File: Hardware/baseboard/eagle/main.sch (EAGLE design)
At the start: 33 parts, among them U3.1 LSM9DS1, X1.0 ARDUINO_UNO, X1.2 TACH/LAP, X2.1 MOTOR

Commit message: stash, added some units
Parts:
- added C1.1: XX, rcl:C-EUC1210K
- added C4.XX1: 100nF, rcl:C-EUC0402K
- added C4.XX10: 2.2uF, rcl:C-EUC0603K
- added C4.XX11, C4.XX12: 100uF, kitt.psvs:CPOL-29172312
- added C4.XX2: 10uF, rcl:C-EUC0603
- added D1.1: (no value), diode:SCHOTTKY-DIODESMD
- added L1: NRS8030XX, kitt.psvs:NRS8030XX
- added L1.1, L2.2: BEAD, rcl:L-EUL4516C
- added R1, R2: (no value), rcl:R-EU_R0805W
- added R4.XX1, R4.XX4, R4.XX5: 100kR, rcl:R-EU_R0402
- added R4.XX2: 549kR, rcl:R-EU_R0402
- added R4.XX3: 90k9R, rcl:R-EU_R0402
- added U☢⏧: TPS61032RSARPSDO-G16, kitt.ic:TPS61032RSARPSDO-G16
- added X2.2: MOTOR, con-phoenix-254:MPT2
- added ☇4XX1⏧: PTR1TP07SQ, testpad:PTR1TP07SQ
- added ☈1, ☈2: (no value), jumper:SJ
- C3.2: value 10nF -> 100nF
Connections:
- removed net AGND: C2.1.2, C2.2.2, C2.3.-, C2.5.2, J2.1.1, U2.2.PGND
- removed net TH: U2.2.PAD
- new net +18V: D1.1.A, R1.2, X2.2-1.1
- new net +5V: L2.2.2
- new net N$1: L1.2, U☢⏧.SW, U☢⏧.SW_2
- new net N$10: U☢⏧.FB, ☇4XX1⏧.TP
- new net N$11: R1.1, R2.2, ☈2.1
- new net N$12: D1.1.C, L1.1.1
- new net N$5: R4.XX1.1, U☢⏧.LBI
- new net N$6: R4.XX2.1, U☢⏧.SYNC
- new net N$7: C4.XX10.1, C4.XX11.+, C4.XX12.+, L2.2.1, U☢⏧.NC, U☢⏧.VOUT, U☢⏧.VOUT_2, U☢⏧.VOUT_3
- new net N$8: R4.XX4.2, U☢⏧.LBO
- new net N$9: R4.XX5.2, U☢⏧.EN
- net GND: now also C1.1.2, C2.1.2, C2.2.2, C2.3.-, C2.5.2, C4.XX1.2, C4.XX10.2, C4.XX11.-, C4.XX12.-, C4.XX2.2, J2.1.1, R2.1, R4.XX3.2, U2.2.PAD, U2.2.PGND, U☢⏧.EP, U☢⏧.GND, U☢⏧.PGND, U☢⏧.PGND_2, U☢⏧.PGND_3, X2.2-2.1
- net VCC/2: now also C1.1.1, C4.XX1.1, C4.XX2.1, L1.1, L1.1.2, R4.XX1.2, R4.XX2.2, R4.XX3.1, U☢⏧.VBAT, ☈1.1
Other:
- note added: "ANNOTATIONS"
- note added: "DO NOT POPULATE"
- note added: "General TODOs: [ ] Figure out where to put a mp/mt switch for switching device off [ ] Add new power chain design before 5V Booster using the LT4000 [ ] Rename all XX identifiers [ ] …???"
- note added: "PfaffM: No point in making separate GND zones, focus on preventing slit antennae"
- note added: "[ ] Check proximity constraints for passives -> Application Note [ ] Important: Double check values and omittables!!! also LB and FB! [ ] Pullups: To which potential? 3V3 seems really fishy, given it comes from the SoC. [ ] Name nets on pins after pins connected for routing later, maybe use some unicode symbol for proximity constraints?"
- note added: "[!!!!!!SHUNTS!!!!!!!!!]"
- note added: "[FILTER FOR UART BURSTS?]"
- note added: "[RAIL MONITORING??]"
- note added: "[TODO:PKG]"

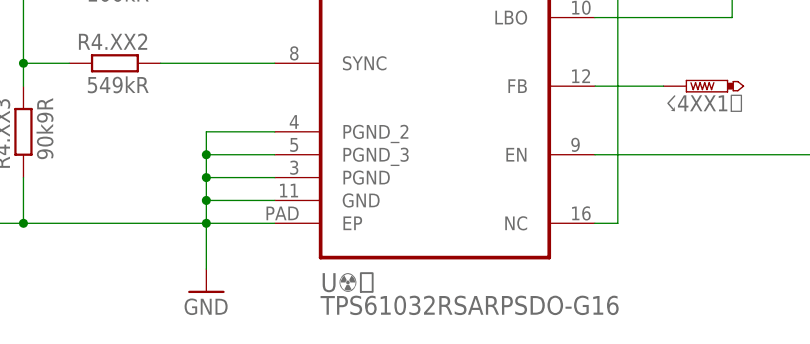
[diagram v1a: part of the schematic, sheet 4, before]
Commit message: Added some more notes and TODOs on guide layer
(also inserted a ☺, shoutout to esdave)
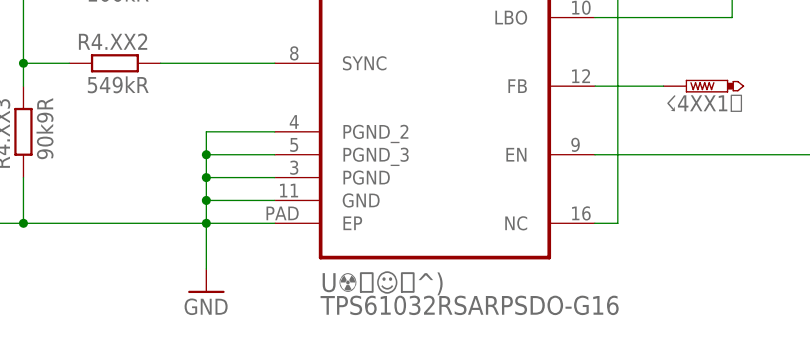
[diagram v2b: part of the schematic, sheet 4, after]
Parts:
- renumbered U☢⏧ to U☢⏧☺˸^)
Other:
- note added: "General TODOs: [ ] Figure out where to put a mp/mt switch for switching device off [ ] Add new power chain design before 5V Booster using the LT4000 [ ] Rename all XX identifiers [ ] Respect Sodd's Second Law[1]: Implement Fail-Safe or Fail-Badly >in hardware<, anything but Fail-Deadly is better than previously"
- note added: "PfaffM(sic): No point in making separate GND zones, focus on preventing slit antennae"
- note added: "[1]: Sodd's Second Law §a; Sooner or later, the worst possible combination of circumstances will happen §b; A system must always be designed to resist the worst possible combination of circumstances"
- note removed: "General TODOs: [ ] Figure out where to put a mp/mt switch for switching device off [ ] Add new power chain design before 5V Booster using the LT4000 [ ] Rename all XX identifiers [ ] …???"
- note removed: "PfaffM: No point in making separate GND zones, focus on preventing slit antennae"
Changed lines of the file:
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@@
 <part name="C2.1" library="rcl" deviceset="C-EU" device="C0805K" value="4.7uF/25V"/>
 <part name="FRAME4" library="frames" deviceset="A4L-LOC" device=""/>
-<part name="U☢⏧" library="kitt.ic" deviceset="TPS61032RSAR" device="PSDO-G16"/>
+<part name="U☢⏧☺˸^)" library="kitt.ic" deviceset="TPS61032RSAR" device="PSDO-G16"/>
 <part name="L1" library="kitt.psvs" deviceset="NRS8030XX" device=""/>
 <part name="P+2" library="supply1" deviceset="VCC/2" device="" value="SYSV"/>
@@
 [  ] Add new power chain design before 5V Booster using the LT4000
 [  ] Rename all XX identifiers
-[  ] …???</text>
+[  ] Respect Sodd's Second Law[1]: Implement Fail-Safe or Fail-Badly &gt;in hardware&lt;, anything but Fail-Deadly is better than previously</text>
 <text x="17.78" y="15.24" size="2.54" layer="114">DO NOT POPULATE</text>
 <rectangle x1="7.62" y1="15.24" x2="15.24" y2="17.78" layer="114"/>
@@
 </text>
 <text x="53.34" y="116.84" size="1.6764" layer="98">[FILTER FOR UART BURSTS?]</text>
+<text x="195.58" y="-20.32" size="1.778" layer="98">[1]: Sodd's Second Law
+§a; Sooner or later, the worst possible combination of
+circumstances will happen
+§b; A system must always be designed to resist the worst
+possible combination of circumstances
+</text>
 </plain>
 <instances>
@@
 [ ] ERC Check
 [ ] Schematic/Peer Review</text>
-<text x="124.46" y="55.88" size="1.778" layer="98">PfaffM: No point in making separate GND zones, focus on preventing slit antennae</text>
+<text x="124.46" y="55.88" size="1.778" layer="98">PfaffM(sic): No point in making separate GND zones, focus on preventing slit antennae</text>
 </plain>
 <instances>
@@
 <instances>
 <instance part="FRAME4" gate="G$1" x="0" y="0"/>
-<instance part="U☢⏧" gate="A" x="119.38" y="101.6"/>
+<instance part="U☢⏧☺˸^)" gate="A" x="119.38" y="101.6"/>
 <instance part="L1" gate="G$1" x="83.82" y="116.84" rot="R90"/>
 <instance part="P+2" gate="G$1" x="45.72" y="121.92"/>
@@
 <net name="N$1" class="0">
 <segment>
-<pinref part="U☢⏧" gate="A" pin="SW"/>
+<pinref part="U☢⏧☺˸^)" gate="A" pin="SW"/>
 <wire x1="101.6" y1="114.3" x2="96.52" y2="114.3" width="0.1524" layer="91"/>
 <wire x1="96.52" y1="114.3" x2="96.52" y2="116.84" width="0.1524" layer="91"/>
-<pinref part="U☢⏧" gate="A" pin="SW_2"/>
+<pinref part="U☢⏧☺˸^)" gate="A" pin="SW_2"/>
 <wire x1="96.52" y1="116.84" x2="101.6" y2="116.84" width="0.1524" layer="91"/>
 <pinref part="L1" gate="G$1" pin="2"/>
@@
 <segment>
 <pinref part="P+2" gate="G$1" pin="VCC/2"/>
-<pinref part="U☢⏧" gate="A" pin="VBAT"/>
+<pinref part="U☢⏧☺˸^)" gate="A" pin="VBAT"/>
 <wire x1="101.6" y1="109.22" x2="73.66" y2="109.22" width="0.1524" layer="91"/>
 <wire x1="73.66" y1="109.22" x2="60.96" y2="109.22" width="0.1524" layer="91"/>
@@
 <segment>
 <pinref part="R4.XX1" gate="G$1" pin="1"/>
-<pinref part="U☢⏧" gate="A" pin="LBI"/>
+<pinref part="U☢⏧☺˸^)" gate="A" pin="LBI"/>
 <wire x1="88.9" y1="104.14" x2="101.6" y2="104.14" width="0.1524" layer="91"/>
 </segment>
@@
 <segment>
 <pinref part="R4.XX2" gate="G$1" pin="1"/>
-<pinref part="U☢⏧" gate="A" pin="SYNC"/>
+<pinref part="U☢⏧☺˸^)" gate="A" pin="SYNC"/>
 <wire x1="88.9" y1="93.98" x2="101.6" y2="93.98" width="0.1524" layer="91"/>
 </segment>
@@
 <net name="GND" class="0">
 <segment>
-<pinref part="U☢⏧" gate="A" pin="EP"/>
+<pinref part="U☢⏧☺˸^)" gate="A" pin="EP"/>
 <pinref part="GND15" gate="1" pin="GND"/>
 <wire x1="101.6" y1="76.2" x2="93.98" y2="76.2" width="0.1524" layer="91"/>
 <wire x1="93.98" y1="76.2" x2="93.98" y2="71.12" width="0.1524" layer="91"/>
-<pinref part="U☢⏧" gate="A" pin="GND"/>
+<pinref part="U☢⏧☺˸^)" gate="A" pin="GND"/>
 <wire x1="101.6" y1="78.74" x2="93.98" y2="78.74" width="0.1524" layer="91"/>
 <wire x1="93.98" y1="78.74" x2="93.98" y2="76.2" width="0.1524" layer="91"/>
 <junction x="93.98" y="76.2"/>
-<pinref part="U☢⏧" gate="A" pin="PGND"/>
+<pinref part="U☢⏧☺˸^)" gate="A" pin="PGND"/>
 <wire x1="101.6" y1="81.28" x2="93.98" y2="81.28" width="0.1524" layer="91"/>
 <wire x1="93.98" y1="81.28" x2="93.98" y2="78.74" width="0.1524" layer="91"/>
 <junction x="93.98" y="78.74"/>
-<pinref part="U☢⏧" gate="A" pin="PGND_3"/>
+<pinref part="U☢⏧☺˸^)" gate="A" pin="PGND_3"/>
 <wire x1="101.6" y1="83.82" x2="93.98" y2="83.82" width="0.1524" layer="91"/>
 <wire x1="93.98" y1="83.82" x2="93.98" y2="81.28" width="0.1524" layer="91"/>
 <junction x="93.98" y="81.28"/>
-<pinref part="U☢⏧" gate="A" pin="PGND_2"/>
+<pinref part="U☢⏧☺˸^)" gate="A" pin="PGND_2"/>
 <wire x1="101.6" y1="86.36" x2="93.98" y2="86.36" width="0.1524" layer="91"/>
 <wire x1="93.98" y1="86.36" x2="93.98" y2="83.82" width="0.1524" layer="91"/>
@@
 <net name="N$7" class="0">
 <segment>
-<pinref part="U☢⏧" gate="A" pin="NC"/>
+<pinref part="U☢⏧☺˸^)" gate="A" pin="NC"/>
 <wire x1="137.16" y1="76.2" x2="139.7" y2="76.2" width="0.1524" layer="91"/>
-<pinref part="U☢⏧" gate="A" pin="VOUT_2"/>
+<pinref part="U☢⏧☺˸^)" gate="A" pin="VOUT_2"/>
 <wire x1="139.7" y1="76.2" x2="139.7" y2="106.68" width="0.1524" layer="91"/>
 <wire x1="139.7" y1="106.68" x2="139.7" y2="114.3" width="0.1524" layer="91"/>
 <wire x1="139.7" y1="114.3" x2="139.7" y2="116.84" width="0.1524" layer="91"/>
 <wire x1="139.7" y1="116.84" x2="137.16" y2="116.84" width="0.1524" layer="91"/>
-<pinref part="U☢⏧" gate="A" pin="VOUT_3"/>
+<pinref part="U☢⏧☺˸^)" gate="A" pin="VOUT_3"/>
 <wire x1="137.16" y1="114.3" x2="139.7" y2="114.3" width="0.1524" layer="91"/>
 <junction x="139.7" y="114.3"/>
-<pinref part="U☢⏧" gate="A" pin="VOUT"/>
+<pinref part="U☢⏧☺˸^)" gate="A" pin="VOUT"/>
 <wire x1="137.16" y1="106.68" x2="139.7" y2="106.68" width="0.1524" layer="91"/>
 <junction x="139.7" y="106.68"/>
@@
 <net name="N$8" class="0">
 <segment>
-<pinref part="U☢⏧" gate="A" pin="LBO"/>
+<pinref part="U☢⏧☺˸^)" gate="A" pin="LBO"/>
 <pinref part="R4.XX4" gate="G$1" pin="2"/>
 <wire x1="137.16" y1="99.06" x2="152.4" y2="99.06" width="0.1524" layer="91"/>
@@
 <net name="N$9" class="0">
 <segment>
-<pinref part="U☢⏧" gate="A" pin="EN"/>
+<pinref part="U☢⏧☺˸^)" gate="A" pin="EN"/>
 <pinref part="R4.XX5" gate="G$1" pin="2"/>
 <wire x1="137.16" y1="83.82" x2="162.56" y2="83.82" width="0.1524" layer="91"/>
@@
 <net name="N$10" class="0">
 <segment>
-<pinref part="U☢⏧" gate="A" pin="FB"/>
+<pinref part="U☢⏧☺˸^)" gate="A" pin="FB"/>
 <pinref part="☇4XX1⏧" gate="G$1" pin="TP"/>
 <wire x1="137.16" y1="91.44" x2="144.78" y2="91.44" width="0.1524" layer="91"/>

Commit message: put LT4000-1 into /baseboard/ schematic , also added some datasheets , and updated the ic library
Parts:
- removed U☢⏧☺˸^): TPS61032RSARPSDO-G16, kitt.ic:TPS61032RSARPSDO-G16
- added C5.XX1, C5.XX5, C5.XX6: F/XX, rcl:C-EU025-024X044
- added C5.XX2: 1uF/XX, rcl:C-EU025-024X044
- added C5.XX3, C5.XX4: 10nF/XX, rcl:C-EU025-024X044
- added L5.XX1: H/XX, rcl:L-EU0204/7
- added P1: JST.S2B-PH-SM4-TB, kitt.con:JST.S2B-PH-SM4-TB
- added Q5.XX1, Q5.XX2, Q5.XX3: PCF/XX, transistor-power:IRF4905
- added R5.XX1: R/XX, rcl:R-EU_0204/5
- added R5.XX10: 82kR/XX, rcl:R-EU_0204/5
- added R5.XX11, R5.XX4, R5.XX5: 100kR/XX, rcl:R-EU_0204/5
- added R5.XX12: 270kR/XX, rcl:R-EU_0204/5
- added R5.XX13: 5mR/XX, rcl:R-EU_0204/5
- added R5.XX2, R5.XX3: 1kR/XX, rcl:R-EU_0204/5
- added R5.XX6: 0.82R/XX, rcl:R-EU_0204/5
- added R5.XX7: 16kR/XX, rcl:R-EU_0204/5
- added R5.XX8: 1MR/XX, rcl:R-EU_0204/5
- added R5.XX9: 220kR/XX, rcl:R-EU_0204/5
- added U4: TPS61032RSARP˸^)SDO-G16, kitt.ic:TPS61032RSARPSDO-G16
- added U5: LTC4000-1, kitt.ic:LTC4000-1
- added ☇5XX1, ☇5XX2, ☇5XX3, ☇5XX4: PTR1TP07SQ, testpad:PTR1TP07SQ
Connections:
- new net BAT.+: Q5.XX3.D, R5.XX9.2, U5.BAT
- new net BAT.NTC: U5.NTC
- new net DDC.!RST: U5.!RST
- new net DDC.IN: Q5.XX2.S, R5.XX6.2, U5.CLN, U5.IID
- new net N$13: R5.XX2.2, U5.CX
- new net N$14: R5.XX3.2, U5.CL
- new net N$15: R5.XX4.1, U5.!CHRG
- new net N$16: R5.XX5.1, U5.!FLT
- new net N$17: C5.XX4.1, U5.IBMON
- new net N$18: C5.XX3.1, U5.IIMON
- new net N$19: C5.XX5.1, R5.XX7.1
- new net N$20: C5.XX5.2, U5.CC
- new net N$21: R5.XX7.2, U5.ITH
- new net N$23: Q5.XX2.G, R5.XX8.2, U5.IGATE
- new net N$24: R5.XX10.1, R5.XX9.1, U5.BFB
- new net N$25: R5.XX10.2, R5.XX11.1, U5.FBG
- new net N$26: R5.XX11.2, R5.XX12.1, U5.OFB
- new net N$27: Q5.XX3.S, R5.XX13.1, U5.CSN
- new net N$28: Q5.XX3.G, U5.BGATE
- new net N5.BIAS: C5.XX2.1, R5.XX4.2, R5.XX5.2, U5.BIAS, U5.VM
- new net N5.ENC: U5.ENC, ☇5XX3.TP
- new net N5.IFB: U5.IFB, ☇5XX4.TP
- new net N5.TMR: U5.TMR, ☇5XX2.TP
- net GND: now also C5.XX2.2, C5.XX3.2, C5.XX4.2, C5.XX6.2, R5.XX2.1, R5.XX3.1, U4.EP, U4.GND, U4.PGND, U4.PGND_2, U4.PGND_3, U5.GND; no longer U☢⏧☺˸^).EP, U☢⏧☺˸^).GND, U☢⏧☺˸^).PGND, U☢⏧☺˸^).PGND_2, U☢⏧☺˸^).PGND_3
- net N$1: now also U4.SW, U4.SW_2; no longer U☢⏧☺˸^).SW, U☢⏧☺˸^).SW_2
- net N$10: now also U4.FB; no longer U☢⏧☺˸^).FB
- net N$5: now also U4.LBI; no longer U☢⏧☺˸^).LBI
- net N$6: now also U4.SYNC; no longer U☢⏧☺˸^).SYNC
- net N$7: now also U4.NC, U4.VOUT, U4.VOUT_2, U4.VOUT_3; no longer U☢⏧☺˸^).NC, U☢⏧☺˸^).VOUT, U☢⏧☺˸^).VOUT_2, U☢⏧☺˸^).VOUT_3
- net N$8: now also U4.LBO; no longer U☢⏧☺˸^).LBO
- net N$9: now also U4.EN; no longer U☢⏧☺˸^).EN
- net VCC/2: now also C5.XX6.1, Q5.XX2.D, R4.XX4.1, R4.XX5.1, R5.XX12.2, R5.XX13.2, R5.XX6.1, R5.XX8.1, U4.VBAT, U5.CSP, U5.IN; no longer U☢⏧☺˸^).VBAT
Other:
- note added: "(TURN OFF)"
- note added: "Refer to [ltc4001 p24s4] "Input Voltage Programming""
- note added: "TODO: Replace all packages of passives (currently non-smt)"
- note added: "TOOLBOX"
- note added: "[TODO 2]"
- note added: "[TODO1] 8.2 milliohms? really? Could calcuate trace resistence for that"
- note added: "[TODO3] Package this and everything else into MODULES. Those seem pretty damn useful."
- note added: "[TODO:1]"
- note added: "ad: Is this Kelvinized, judging by the wires?"
- note added: "refer to: ../sim/Supply/LTC4000_V1.asc"

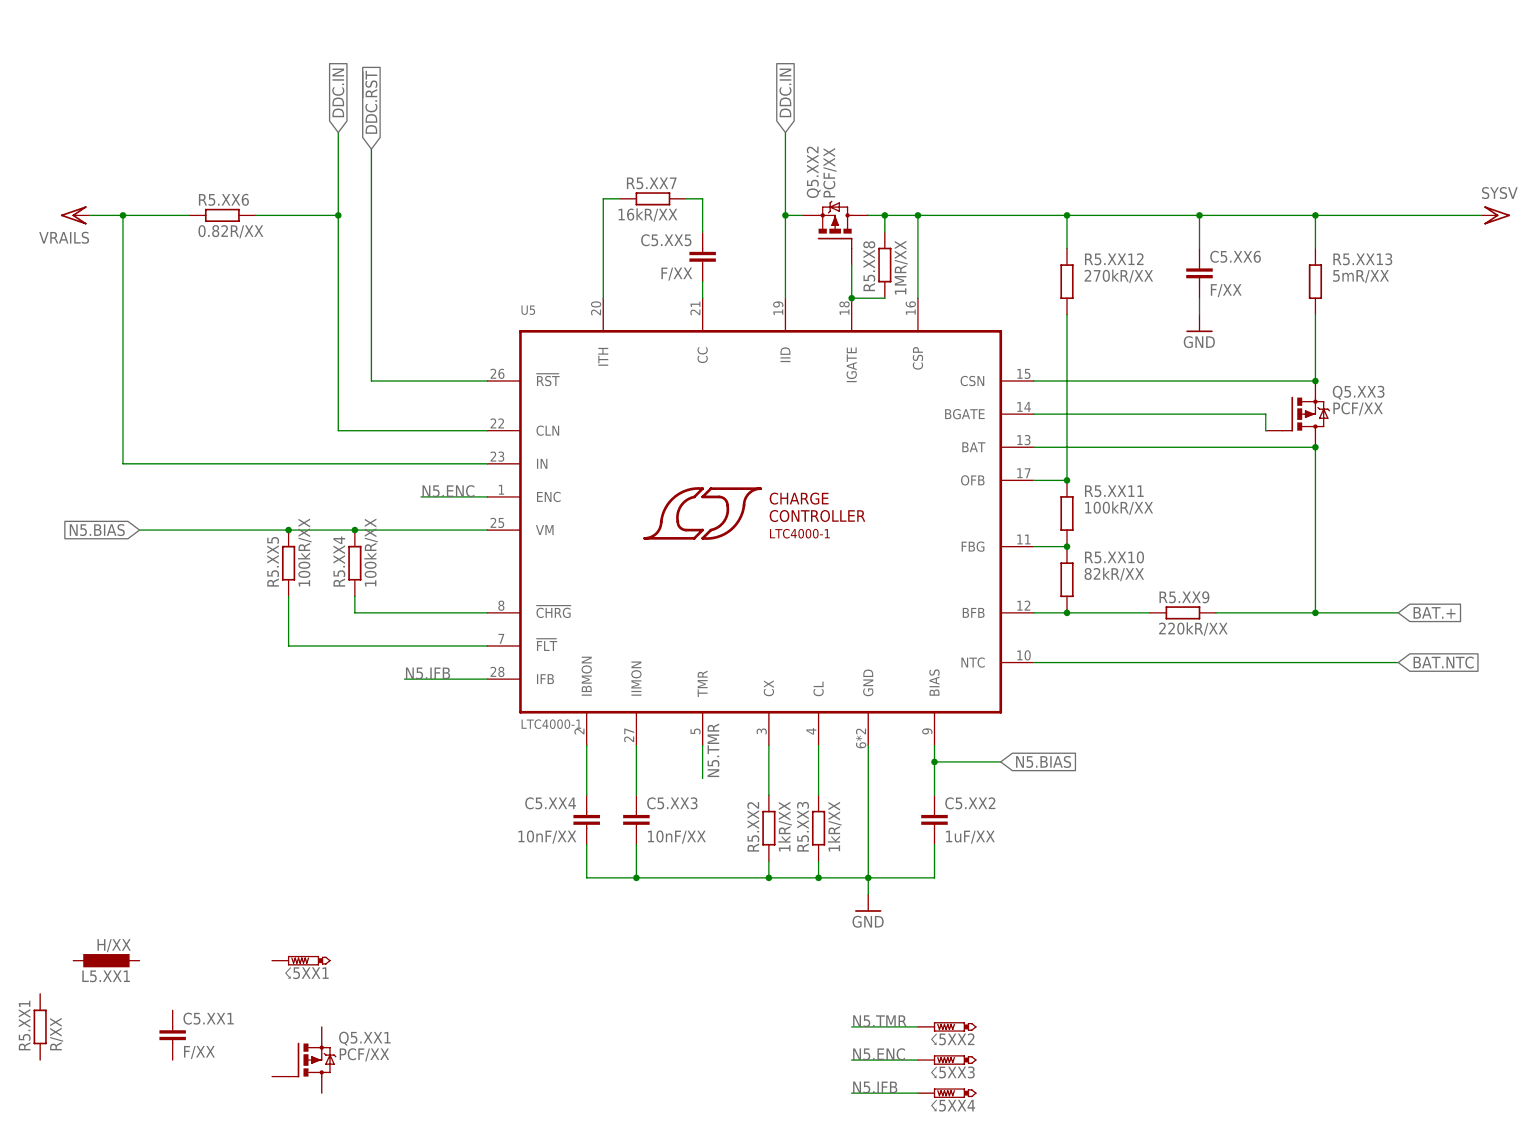
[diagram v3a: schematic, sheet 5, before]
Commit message: added some testpoints just in case , most of which are taken from the datasheet , which will provide a good reference in case of yet another murphy incident
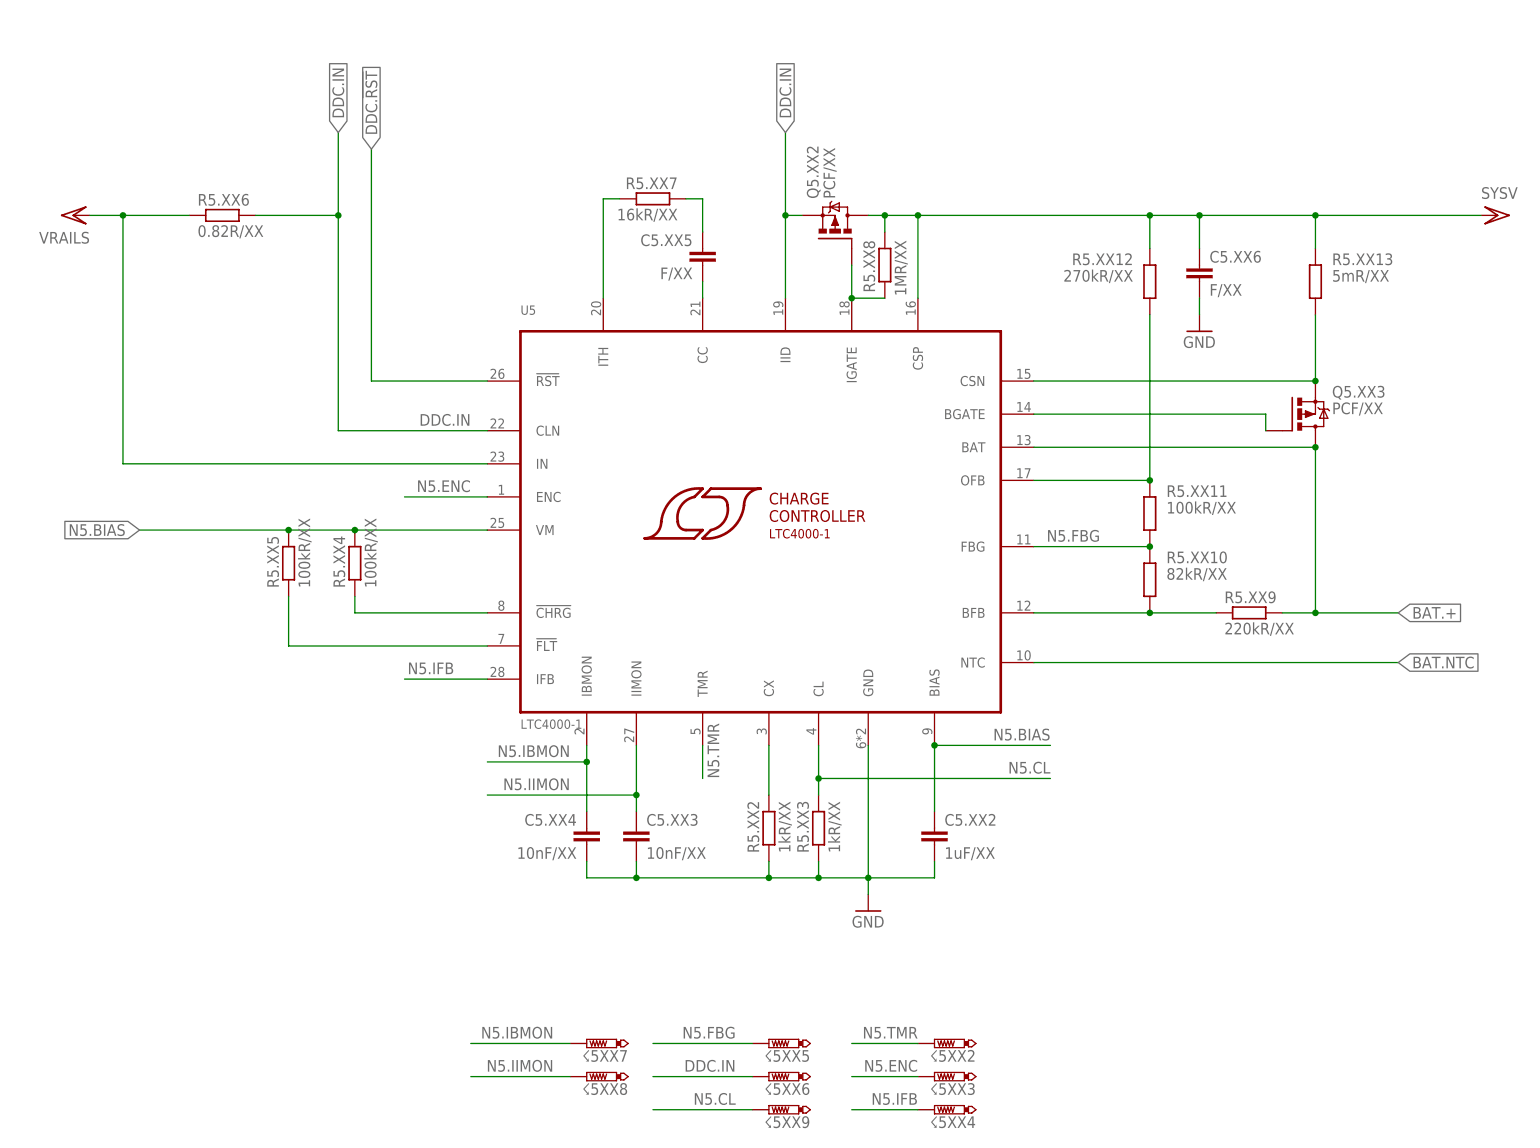
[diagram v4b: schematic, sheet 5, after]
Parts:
- removed C5.XX1: F/XX, rcl:C-EU025-024X044
- removed L5.XX1: H/XX, rcl:L-EU0204/7
- removed Q5.XX1: PCF/XX, transistor-power:IRF4905
- removed R5.XX1: R/XX, rcl:R-EU_0204/5
- removed ☇5XX1: PTR1TP07SQ, testpad:PTR1TP07SQ
- added ☇5XX5, ☇5XX6, ☇5XX7, ☇5XX8, ☇5XX9: PTR1TP07SQ, testpad:PTR1TP07SQ
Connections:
- removed net N$14: R5.XX3.2, U5.CL
- removed net N$17: C5.XX4.1, U5.IBMON
- removed net N$18: C5.XX3.1, U5.IIMON
- removed net N$25: R5.XX10.2, R5.XX11.1, U5.FBG
- new net N5.CL: R5.XX3.2, U5.CL, ☇5XX9.TP
- new net N5.FBG: R5.XX10.2, R5.XX11.1, U5.FBG, ☇5XX5.TP
- new net N5.IBMON: C5.XX4.1, U5.IBMON, ☇5XX7.TP
- new net N5.IIMON: C5.XX3.1, U5.IIMON, ☇5XX8.TP
- net DDC.IN: now also ☇5XX6.TP
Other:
- note removed: "TOOLBOX"
- moved on the sheet: C5.XX2, C5.XX3, C5.XX4, R5.XX10, R5.XX11, R5.XX12, R5.XX9, ☇5XX2, ☇5XX3, ☇5XX4
